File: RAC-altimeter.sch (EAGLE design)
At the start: 20 parts, among them IC1 BMI088, IC2 BMP388, IC3 STM32L412KBU6, IC4 TPS73733DCQR, J1 MICRO-SD

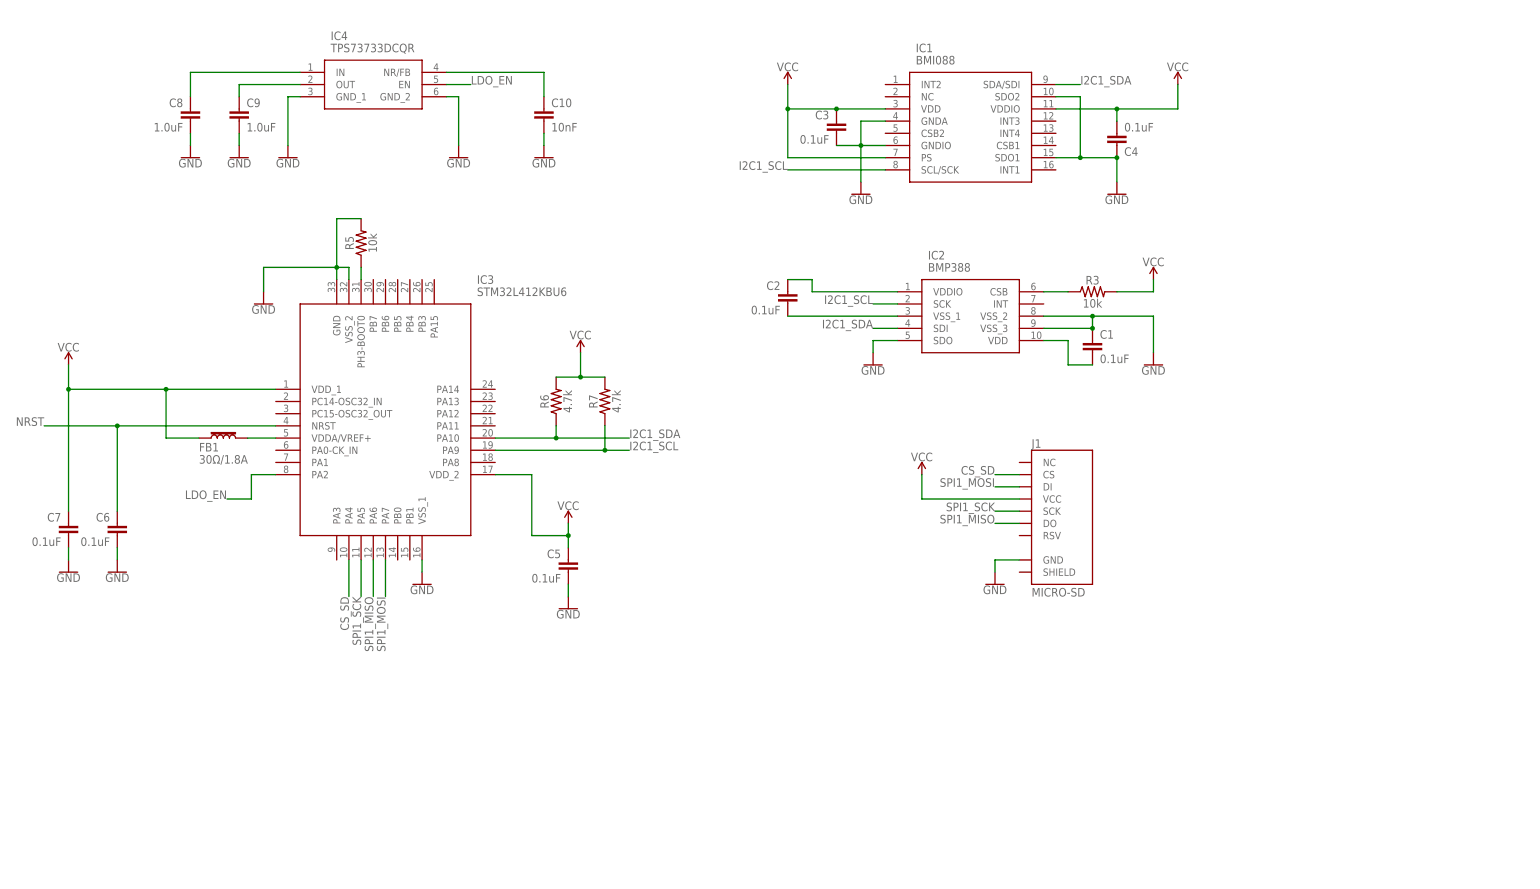
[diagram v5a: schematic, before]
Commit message: Re-integrated the MAX32660 in a 20-pin package
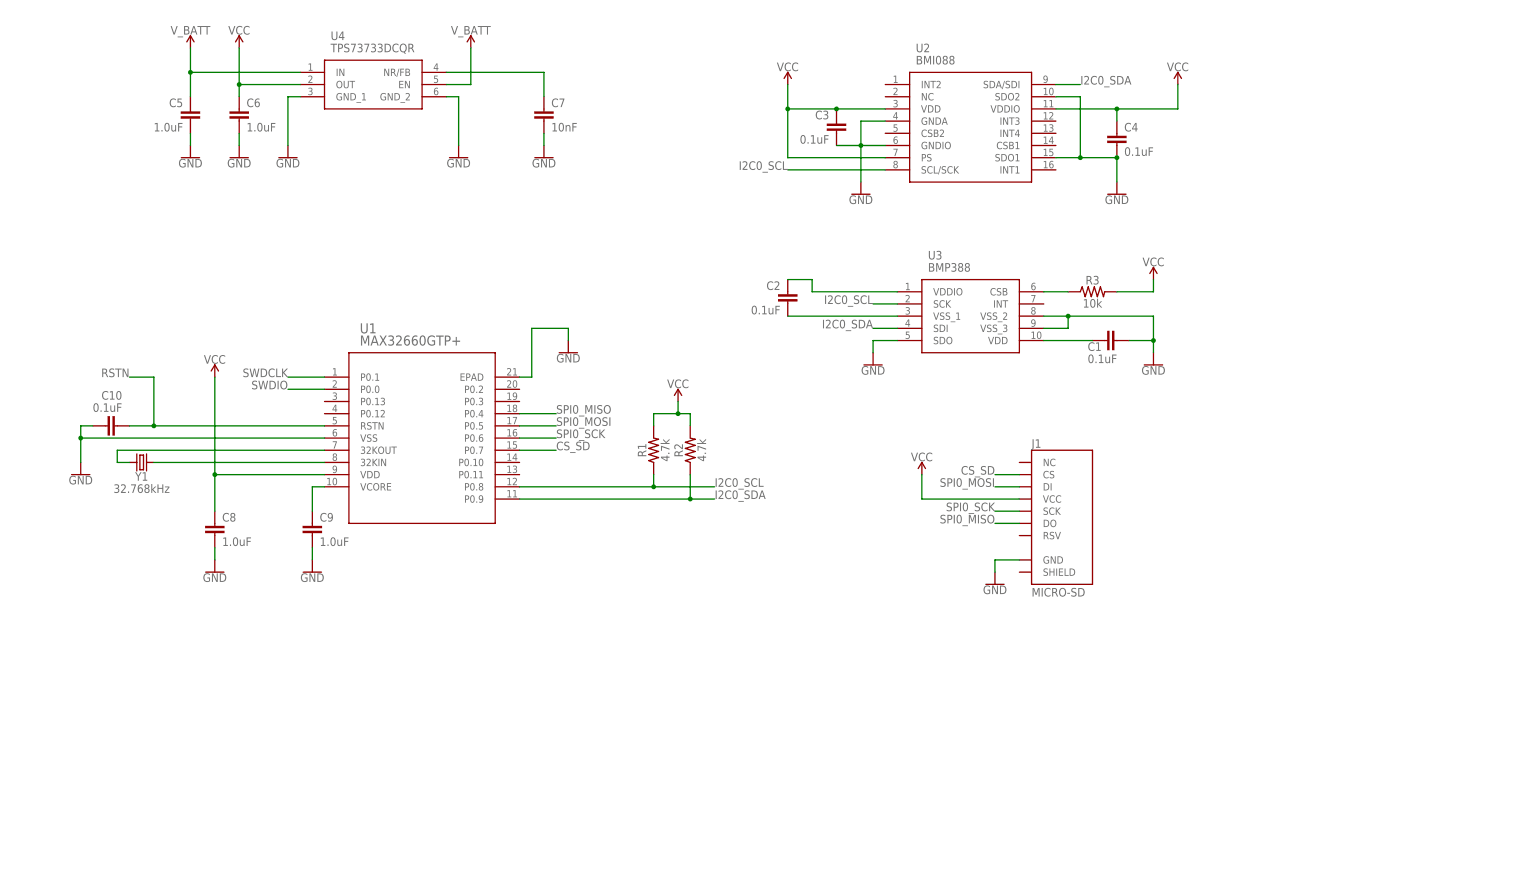
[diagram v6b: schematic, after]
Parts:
- removed FB1: 30Ω/1.8A, SparkFun-Coils:FERRITE_BEAD-0603
- removed IC3: STM32L412KBU6, STM32L412KBU6:STM32L412KBU6
- removed R5: 10k, SparkFun-Resistors:10KOHM-0603-1/10W-1%
- removed R6, R7: 4.7k, SparkFun-Resistors:4.7KOHM-0603-1/10W-1%
- added R1, R2: 4.7k, SparkFun-Resistors:4.7KOHM-0603-1/10W-1%
- added U1: MAX32660GTP+, RAC-Altimeter:MAX32660GTP+
- added Y1: 32.768kHz, SparkFun-Clocks:CRYSTAL-32.768KHZSMD-3.2X1.5
- C10: value 10nF -> 0.1uF; device SparkFun-Capacitors:10NF-0603-50V-10% -> SparkFun-Capacitors:0.1UF-0603-25V-(+80/-20%)
- C5, C6: value 0.1uF -> 1.0uF; device SparkFun-Capacitors:0.1UF-0603-25V-(+80/-20%) -> SparkFun-Capacitors:1.0UF-0603-16V-10%
- C7: value 0.1uF -> 10nF; device SparkFun-Capacitors:0.1UF-0603-25V-(+80/-20%) -> SparkFun-Capacitors:10NF-0603-50V-10%
- renumbered IC1 to U2, IC2 to U3, IC4 to U4
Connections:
- removed net I2C1_SCL: IC3.PA9, R7.1, U2.SCL/SCK, U3.SCK
- removed net I2C1_SDA: IC3.PA10, R6.1, U2.SDA/SDI, U3.SDI
- removed net LDO_EN: IC3.PA2, U4.EN
- removed net N$1: C8.1, U4.IN
- removed net N$2: C9.1, U4.OUT
- removed net N$3: IC3.PH3-BOOT0, R5.1
- removed net N$7: FB1.2, IC3.VDDA/VREF+
- removed net NRST: C6.1, IC3.NRST
- removed net SPI1_MISO: IC3.PA6, J1.DO
- removed net SPI1_MOSI: IC3.PA7, J1.DI
- removed net SPI1_SCK: IC3.PA5, J1.SCK
- new net I2C0_SCL: R1.1, U1.P0.8, U2.SCL/SCK, U3.SCK
- new net I2C0_SDA: R2.1, U1.P0.9, U2.SDA/SDI, U3.SDI
- new net N$10: U1.32KOUT, Y1.2
- new net N$11: C9.1, U1.VCORE
- new net N$9: U1.32KIN, Y1.1
- new net RSTN: C10.1, U1.RSTN
- new net SPI0_MISO: J1.DO, U1.P0.4
- new net SPI0_MOSI: J1.DI, U1.P0.5
- new net SPI0_SCK: J1.SCK, U1.P0.6
- new net SWDCLK: U1.P0.1
- new net SWDIO: U1.P0.0
- new net V_BATT: C5.1, U4.EN, U4.IN
- net CS_SD: now also U1.P0.7; no longer IC3.PA4
- net GND: now also U1.EPAD, U1.VSS; no longer IC3.GND, IC3.VSS_1, IC3.VSS_2, R5.2
- net N$8: now also C7.1; no longer C10.1
- net VCC: now also C6.1, C8.1, R1.2, R2.2, U1.VDD, U4.OUT; no longer C5.1, C7.1, FB1.1, IC3.VDD_1, IC3.VDD_2, R6.2, R7.2
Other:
- moved on the sheet: C1, C10, C5, C6, C7, C8, C9

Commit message: Integrated the RN4871 bluetooth module
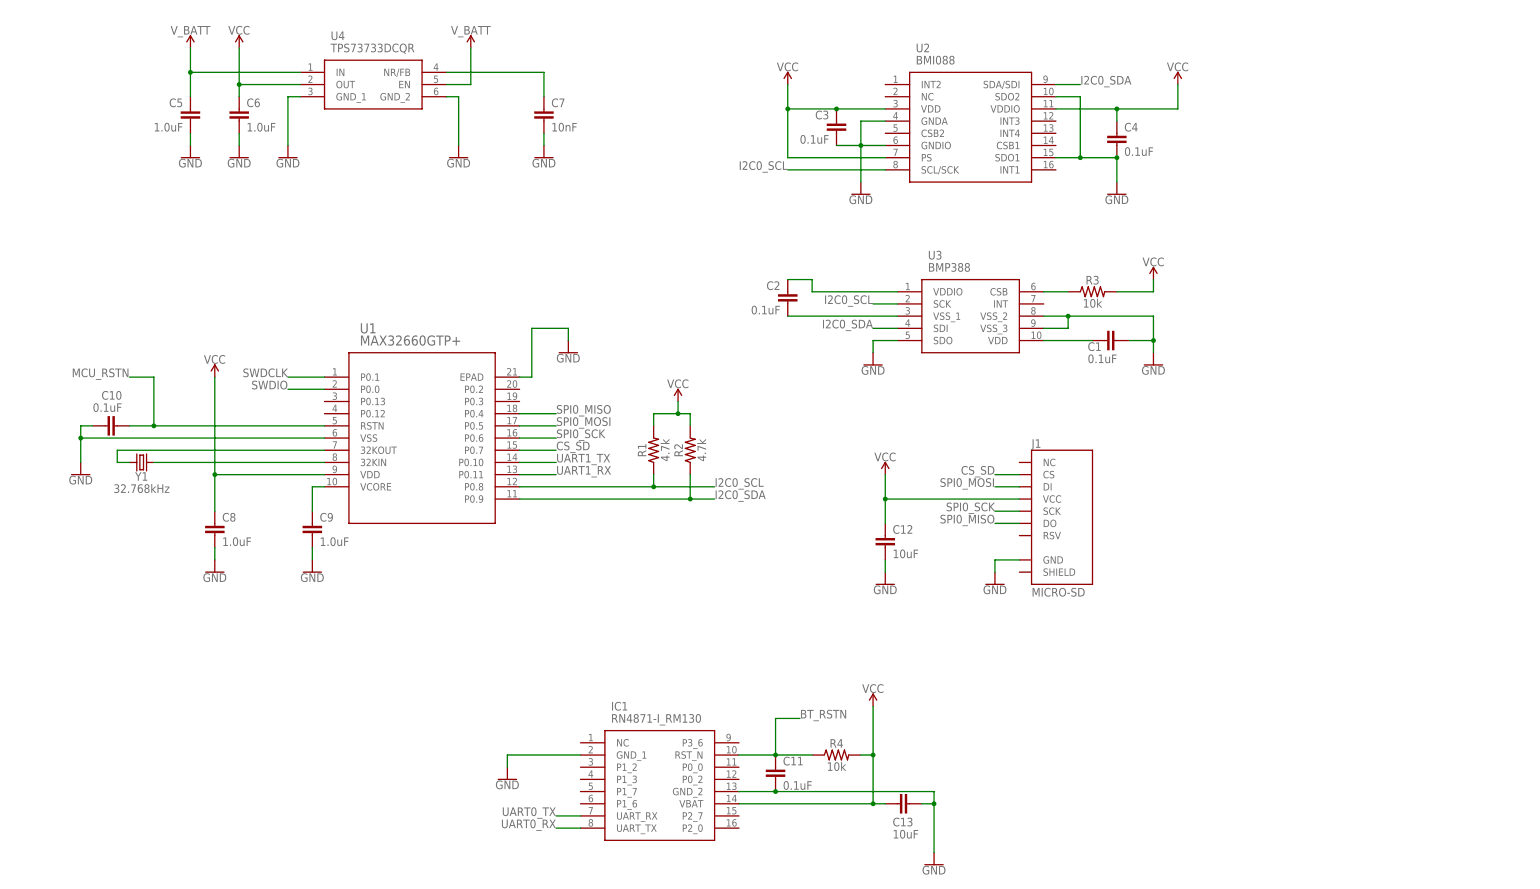
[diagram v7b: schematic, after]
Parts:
- added C11: 0.1uF, SparkFun-Capacitors:0.1UF-0603-25V-(+80/-20%)
- added C12, C13: 10uF, SparkFun-Capacitors:10UF-0603-6.3V-20%
- added IC1: RN4871-I_RM130, RAC-Altimeter:RN4871-I_RM130
- added R4: 10k, SparkFun-Resistors:10KOHM-0603-1/10W-1%
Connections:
- net RSTN renamed MCU_RSTN
- new net BT_RSTN: C11.1, IC1.RST_N, R4.1
- new net UART0_RX: IC1.UART_TX
- new net UART0_TX: IC1.UART_RX
- new net UART1_RX: U1.P0.11
- new net UART1_TX: U1.P0.10
- net GND: now also C11.2, C12.2, C13.2, IC1.GND_1, IC1.GND_2
- net VCC: now also C12.1, C13.1, IC1.VBAT, R4.2
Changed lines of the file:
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@@
 <part name="SUPPLY6" library="SparkFun-PowerSymbols" deviceset="V_BATT" device=""/>
 <part name="SUPPLY7" library="SparkFun-PowerSymbols" deviceset="V_BATT" device=""/>
+<part name="IC1" library="RAC-Altimeter" deviceset="RN4871-I_RM130" device=""/>
+<part name="GND7" library="SparkFun-PowerSymbols" deviceset="GND" device=""/>
+<part name="GND9" library="SparkFun-PowerSymbols" deviceset="GND" device=""/>
+<part name="C12" library="SparkFun-Capacitors" library_urn="urn:adsk.eagle:library:510" deviceset="10UF" device="-0603-6.3V-20%" package3d_urn="urn:adsk.eagle:package:37414/1" value="10uF"/>
+<part name="C13" library="SparkFun-Capacitors" library_urn="urn:adsk.eagle:library:510" deviceset="10UF" device="-0603-6.3V-20%" package3d_urn="urn:adsk.eagle:package:37414/1" value="10uF"/>
+<part name="GND10" library="SparkFun-PowerSymbols" deviceset="GND" device=""/>
+<part name="SUPPLY10" library="SparkFun-PowerSymbols" deviceset="VCC" device=""/>
+<part name="R4" library="SparkFun-Resistors" library_urn="urn:adsk.eagle:library:532" deviceset="10KOHM" device="-0603-1/10W-1%" package3d_urn="urn:adsk.eagle:package:39650/1" value="10k"/>
+<part name="C11" library="SparkFun-Capacitors" deviceset="0.1UF" device="-0603-25V-(+80/-20%)" value="0.1uF"/>
 </parts>
 <sheets>
@@
 <attribute name="VALUE" x="154.94" y="17.526" size="1.778" layer="96" align="top-center"/>
 </instance>
-<instance part="SUPPLY2" gate="G$1" x="139.7" y="40.64" smashed="yes">
-<attribute name="VALUE" x="139.7" y="43.434" size="1.778" layer="96" align="bottom-center"/>
+<instance part="SUPPLY2" gate="G$1" x="132.08" y="40.64" smashed="yes">
+<attribute name="VALUE" x="132.08" y="43.434" size="1.778" layer="96" align="bottom-center"/>
 </instance>
 <instance part="GND3" gate="1" x="129.54" y="63.5" smashed="yes">
@@
 <instance part="SUPPLY7" gate="G$1" x="45.72" y="129.54" smashed="yes">
 <attribute name="VALUE" x="45.72" y="132.334" size="1.778" layer="96" align="bottom-center"/>
+</instance>
+<instance part="IC1" gate="G$1" x="68.58" y="-15.24" smashed="yes">
+<attribute name="NAME" x="74.93" y="-7.62" size="1.778" layer="95" align="center-left"/>
+<attribute name="VALUE" x="74.93" y="-10.16" size="1.778" layer="96" align="center-left"/>
+</instance>
+<instance part="GND7" gate="1" x="53.34" y="-22.86" smashed="yes">
+<attribute name="VALUE" x="53.34" y="-23.114" size="1.778" layer="96" align="top-center"/>
+</instance>
+<instance part="GND9" gate="1" x="142.24" y="-40.64" smashed="yes">
+<attribute name="VALUE" x="142.24" y="-40.894" size="1.778" layer="96" align="top-center"/>
+</instance>
+<instance part="C12" gate="G$1" x="132.08" y="25.4" smashed="yes">
+<attribute name="NAME" x="133.604" y="28.321" size="1.778" layer="95" font="vector"/>
+<attribute name="VALUE" x="133.604" y="23.241" size="1.778" layer="96" font="vector"/>
+</instance>
+<instance part="C13" gate="G$1" x="137.16" y="-27.94" smashed="yes" rot="MR270">
+<attribute name="NAME" x="133.604" y="-30.861" size="1.778" layer="95" font="vector" rot="MR180"/>
+<attribute name="VALUE" x="133.604" y="-33.401" size="1.778" layer="96" font="vector" rot="MR180"/>
+</instance>
+<instance part="GND10" gate="1" x="132.08" y="17.78" smashed="yes">
+<attribute name="VALUE" x="132.08" y="17.526" size="1.778" layer="96" align="top-center"/>
+</instance>
+<instance part="SUPPLY10" gate="G$1" x="129.54" y="-7.62" smashed="yes">
+<attribute name="VALUE" x="129.54" y="-4.826" size="1.778" layer="96" align="bottom-center"/>
+</instance>
+<instance part="R4" gate="G$1" x="121.92" y="-17.78" smashed="yes">
+<attribute name="NAME" x="121.92" y="-16.256" size="1.778" layer="95" font="vector" align="bottom-center"/>
+<attribute name="VALUE" x="121.92" y="-19.304" size="1.778" layer="96" font="vector" align="top-center"/>
+</instance>
+<instance part="C11" gate="G$1" x="109.22" y="-22.86" smashed="yes">
+<attribute name="NAME" x="110.744" y="-19.939" size="1.778" layer="95" font="vector"/>
+<attribute name="VALUE" x="110.744" y="-25.019" size="1.778" layer="96" font="vector"/>
 </instance>
 </instances>
@@
 <wire x1="-7.62" y1="22.86" x2="-7.62" y2="25.4" width="0.1524" layer="91"/>
 </segment>
+<segment>
+<pinref part="IC1" gate="G$1" pin="GND_2"/>
+<pinref part="GND9" gate="1" pin="GND"/>
+<wire x1="101.6" y1="-25.4" x2="109.22" y2="-25.4" width="0.1524" layer="91"/>
+<wire x1="109.22" y1="-25.4" x2="142.24" y2="-25.4" width="0.1524" layer="91"/>
+<wire x1="142.24" y1="-25.4" x2="142.24" y2="-27.94" width="0.1524" layer="91"/>
+<pinref part="C13" gate="G$1" pin="2"/>
+<wire x1="142.24" y1="-27.94" x2="142.24" y2="-38.1" width="0.1524" layer="91"/>
+<wire x1="139.7" y1="-27.94" x2="142.24" y2="-27.94" width="0.1524" layer="91"/>
+<junction x="142.24" y="-27.94"/>
+<pinref part="C11" gate="G$1" pin="2"/>
+<junction x="109.22" y="-25.4"/>
+</segment>
+<segment>
+<pinref part="IC1" gate="G$1" pin="GND_1"/>
+<wire x1="68.58" y1="-17.78" x2="53.34" y2="-17.78" width="0.1524" layer="91"/>
+<pinref part="GND7" gate="1" pin="GND"/>
+<wire x1="53.34" y1="-17.78" x2="53.34" y2="-20.32" width="0.1524" layer="91"/>
+</segment>
+<segment>
+<pinref part="C12" gate="G$1" pin="2"/>
+<pinref part="GND10" gate="1" pin="GND"/>
+<wire x1="132.08" y1="22.86" x2="132.08" y2="20.32" width="0.1524" layer="91"/>
+</segment>
 </net>
 <net name="I2C0_SCL" class="0">
@@
 <segment>
 <pinref part="J1" gate="J1" pin="VCC"/>
-<wire x1="160.02" y1="35.56" x2="139.7" y2="35.56" width="0.1524" layer="91"/>
+<wire x1="160.02" y1="35.56" x2="132.08" y2="35.56" width="0.1524" layer="91"/>
 <pinref part="SUPPLY2" gate="G$1" pin="VCC"/>
-<wire x1="139.7" y1="35.56" x2="139.7" y2="40.64" width="0.1524" layer="91"/>
+<wire x1="132.08" y1="35.56" x2="132.08" y2="40.64" width="0.1524" layer="91"/>
+<pinref part="C12" gate="G$1" pin="1"/>
+<wire x1="132.08" y1="30.48" x2="132.08" y2="35.56" width="0.1524" layer="91"/>
+<junction x="132.08" y="35.56"/>
 </segment>
 <segment>
@@
 <junction x="-2.54" y="121.92"/>
 </segment>
+<segment>
+<pinref part="IC1" gate="G$1" pin="VBAT"/>
+<wire x1="101.6" y1="-27.94" x2="129.54" y2="-27.94" width="0.1524" layer="91"/>
+<pinref part="SUPPLY10" gate="G$1" pin="VCC"/>
+<wire x1="129.54" y1="-27.94" x2="129.54" y2="-17.78" width="0.1524" layer="91"/>
+<pinref part="C13" gate="G$1" pin="1"/>
+<wire x1="129.54" y1="-17.78" x2="129.54" y2="-7.62" width="0.1524" layer="91"/>
+<wire x1="129.54" y1="-27.94" x2="132.08" y2="-27.94" width="0.1524" layer="91"/>
+<junction x="129.54" y="-27.94"/>
+<pinref part="R4" gate="G$1" pin="2"/>
+<wire x1="127" y1="-17.78" x2="129.54" y2="-17.78" width="0.1524" layer="91"/>
+<junction x="129.54" y="-17.78"/>
+</segment>
 </net>
 <net name="N$5" class="0">
@@
 </segment>
 </net>
-<net name="RSTN" class="0">
+<net name="MCU_RSTN" class="0">
 <segment>
 <pinref part="U1" gate="A" pin="RSTN"/>
@@
 </segment>
 </net>
+<net name="BT_RSTN" class="0">
+<segment>
+<pinref part="IC1" gate="G$1" pin="RST_N"/>
+<pinref part="R4" gate="G$1" pin="1"/>
+<wire x1="101.6" y1="-17.78" x2="109.22" y2="-17.78" width="0.1524" layer="91"/>
+<pinref part="C11" gate="G$1" pin="1"/>
+<wire x1="109.22" y1="-17.78" x2="116.84" y2="-17.78" width="0.1524" layer="91"/>
+<junction x="109.22" y="-17.78"/>
+<wire x1="109.22" y1="-17.78" x2="109.22" y2="-10.16" width="0.1524" layer="91"/>
+<wire x1="109.22" y1="-10.16" x2="114.3" y2="-10.16" width="0.1524" layer="91"/>
+<label x="114.3" y="-10.16" size="1.778" layer="95"/>
+</segment>
+</net>
+<net name="UART1_TX" class="0">
+<segment>
+<pinref part="U1" gate="A" pin="P0.10"/>
+<wire x1="55.88" y1="43.18" x2="63.5" y2="43.18" width="0.1524" layer="91"/>
+<label x="63.5" y="43.18" size="1.778" layer="95"/>
+</segment>
+</net>
+<net name="UART1_RX" class="0">
+<segment>
+<pinref part="U1" gate="A" pin="P0.11"/>
+<wire x1="55.88" y1="40.64" x2="63.5" y2="40.64" width="0.1524" layer="91"/>
+<label x="63.5" y="40.64" size="1.778" layer="95"/>
+</segment>
+</net>
+<net name="UART0_TX" class="0">
+<segment>
+<pinref part="IC1" gate="G$1" pin="UART_RX"/>
+<wire x1="68.58" y1="-30.48" x2="63.5" y2="-30.48" width="0.1524" layer="91"/>
+<label x="63.5" y="-30.48" size="1.778" layer="95" rot="MR0"/>
+</segment>
+</net>
+<net name="UART0_RX" class="0">
+<segment>
+<pinref part="IC1" gate="G$1" pin="UART_TX"/>
+<wire x1="68.58" y1="-33.02" x2="63.5" y2="-33.02" width="0.1524" layer="91"/>
+<label x="63.5" y="-33.02" size="1.778" layer="95" rot="MR0"/>
+</segment>
+</net>
